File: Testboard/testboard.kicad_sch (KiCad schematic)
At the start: 0 parts

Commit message: :sparkles: Create the schematic for the testboard
Mostly copied from the original schematic.
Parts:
- added C1, C3, C5, C6, C7: 100n, Capacitor_THT:C_Disc_D4.3mm_W1.9mm_P5.00mm, symbol Device:C
- added C2, C4: 10n, Capacitor_THT:C_Disc_D4.3mm_W1.9mm_P5.00mm, symbol Device:C
- added D1: rt, LED_THT:LED_D3.0mm, symbol Device:LED
- added J1: upper, Connector_PinSocket_2.54mm:PinSocket_2x02_P2.54mm_Vertical, symbol Connector_Generic:Conn_02x02_Odd_Even
- added J2: lower, Connector_PinSocket_2.54mm:PinSocket_2x02_P2.54mm_Vertical, symbol Connector_Generic:Conn_02x02_Odd_Even
- added J3, J4: Out, Connector_PinHeader_2.54mm:PinHeader_1x02_P2.54mm_Vertical, symbol Connector_Generic:Conn_01x02
- added J5: V_{drive}, Connector_PinHeader_2.54mm:PinHeader_1x02_P2.54mm_Vertical, symbol Connector_Generic:Conn_01x02
- added Q1: BC547, Package_TO_SOT_THT:TO-92_Inline, symbol Transistor_BJT:BC547
- added R1: 100R, Resistor_THT:R_Axial_DIN0207_L6.3mm_D2.5mm_P7.62mm_Horizontal, symbol Device:R
- added R10, R9: 1k, Resistor_THT:R_Axial_DIN0207_L6.3mm_D2.5mm_P7.62mm_Horizontal, symbol Device:R
- added R2, R7: 2k2, Resistor_THT:R_Axial_DIN0207_L6.3mm_D2.5mm_P7.62mm_Horizontal, symbol Device:R
- added R3, R4, R8: 10k, Resistor_THT:R_Axial_DIN0207_L6.3mm_D2.5mm_P7.62mm_Horizontal, symbol Device:R
- added R5: 4k7, Resistor_THT:R_Axial_DIN0207_L6.3mm_D2.5mm_P7.62mm_Horizontal, symbol Device:R
- added R6: 470R, Resistor_THT:R_Axial_DIN0207_L6.3mm_D2.5mm_P7.62mm_Horizontal, symbol Device:R
- added RV1: 1M, Potentiometer_THT:Potentiometer_Piher_PT-10-V10_Vertical, symbol Device:R_Potentiometer
- added SW1: SW_Push, Button_Switch_Keyboard:SW_Cherry_MX_1.00u_PCB, symbol Switch:SW_Push
- added SW2: ON/ON, moPsy:PB_Hor_7x7_2pole_2.5mm, symbol Switch:SW_SPDT
- added TP1: IN, TestPoint:TestPoint_Loop_D1.80mm_Drill1.0mm_Beaded, symbol Connector:TestPoint
- added TP2: TRIGGER_IN, TestPoint:TestPoint_Loop_D1.80mm_Drill1.0mm_Beaded, symbol Connector:TestPoint
- added TP3: TR, TestPoint:TestPoint_Loop_D1.80mm_Drill1.0mm_Beaded, symbol Connector:TestPoint
- added TP4: TRIGGER_OUT, TestPoint:TestPoint_Loop_D1.80mm_Drill1.0mm_Beaded, symbol Connector:TestPoint
- added TP5: OUT, TestPoint:TestPoint_Loop_D1.80mm_Drill1.0mm_Beaded, symbol Connector:TestPoint
- added U1: LM555xN, Package_DIP:DIP-8_W7.62mm, symbol Timer:LM555xN
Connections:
- new net: Q1.2 (B), R7.2
- new net: C3.1, R4.1, U1.4 (R)
- new net: Q1.3 (E), R10.1, R8.2, R9.1
- new net: C5.1, C6.1, R5.1, U1.6 (THR), U1.7 (DIS)
- new net: D1.2 (A), R6.1
- new net: R5.2, RV1.2
- new net: J4.1 (Pin_1), R10.2
- new net: C2.2, R3.1, SW2.2 (B), TP3.1, U1.2 (TR)
- new net: R1.1, SW1.2, TP1.1
- new net: J3.1 (Pin_1), R9.2, TP5.1
- new net: C4.1, U1.5 (CV)
- new net: J5.2 (Pin_2), Q1.1 (C)
- new net +12V: C7.1, J1.3 (Pin_3), J1.4 (Pin_4), J5.1 (Pin_1), R2.2, R3.2, R4.2, RV1.1, U1.8 (VCC)
- new net GND: C1.1, C3.2, C4.2, C5.2, C6.2, C7.2, D1.1 (K), J2.1 (Pin_1), J2.2 (Pin_2), J3.2 (Pin_2), J4.2 (Pin_2), R8.1, SW1.1, U1.1 (GND)
- new net TRIGGER_IN: C1.2, C2.1, R1.2, R2.1, SW2.1 (A), TP2.1
- new net TRIGGER_OUT: R6.2, R7.1, TP4.1, U1.3 (Q)
- no-connect marks 0 -> 6
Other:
- note added: "1ms - 250ms"
- note added: "Close to disable HPF, enables Gate mode"
- note added: "Gate/Trigger Output"
- note added: "HPF"
- note added: "LPF"
- note added: "Manual Input"
- note added: "Min Gate / Trigger Length"
- note added: "Power Supply"
- note added: "Trigger Length Selector"
- note added: "pull-up at the gate generator"

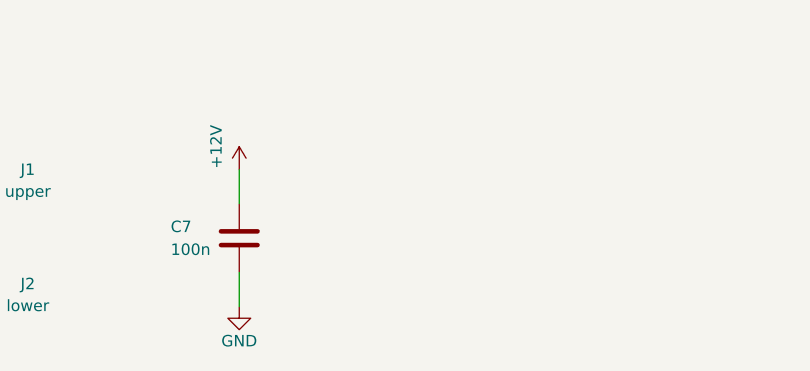
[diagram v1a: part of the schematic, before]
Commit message: :art: Add a GND testpoint for oscilloscope measurements
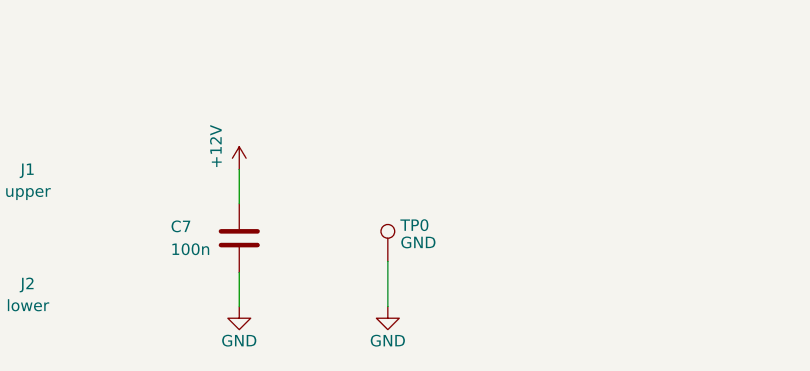
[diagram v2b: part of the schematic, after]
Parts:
- added TP0: GND, TestPoint:TestPoint_Loop_D1.80mm_Drill1.0mm_Beaded, symbol Connector:TestPoint
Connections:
- net GND: now also TP0.1
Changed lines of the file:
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@@
+    (stroke (width 0) (type default))
+  )
+  (wire (pts (xy 97.155 170.18) (xy 97.155 175.26))
     (stroke (width 0) (type default))
   )
@@
         (path "/64d6412c-bfad-42df-9ed7-bcc6cbff0470/a8014c65-0c58-4251-9031-5c5e91cdfe2c"
           (reference "RV7") (unit 1)
+        )
+      )
+    )
+  )
+  (symbol (lib_id "Connector:TestPoint") (at 97.155 170.18 0) (unit 1)
+    (in_bom yes) (on_board yes) (dnp no) (fields_autoplaced)
+    (property "Reference" "TP0" (at 98.552 166.2343 0)
+      (effects (font (size 1.27 1.27)) (justify left))
+    )
+    (property "Value" "GND" (at 98.552 168.1553 0)
+      (effects (font (size 1.27 1.27)) (justify left))
+    )
+    (property "Footprint" "TestPoint:TestPoint_Loop_D1.80mm_Drill1.0mm_Beaded" (at 102.235 170.18 0)
+      (effects (font (size 1.27 1.27)) hide)
+    )
+    (property "Datasheet" "~" (at 102.235 170.18 0)
+      (effects (font (size 1.27 1.27)) hide)
+    )
+    (pin "1")
+    (instances
+      (project "testboard"
+        (path "/1c5578e4-330a-41ae-a1d1-d71bb4a1a163"
+          (reference "TP0") (unit 1)
         )
       )
@@
         )
       )
+    )
+  )
+  (symbol (lib_id "power:GND") (at 97.155 175.26 0) (unit 1)
+    (in_bom yes) (on_board yes) (dnp no)
+    (property "Reference" "#PWR011" (at 97.155 181.61 0)
+      (effects (font (size 1.27 1.27)) hide)
+    )
+    (property "Value" "GND" (at 97.155 179.07 0)
+      (effects (font (size 1.27 1.27)))
+    )
+    (property "Footprint" "" (at 97.155 175.26 0)
+      (effects (font (size 1.27 1.27)) hide)
+    )
+    (property "Datasheet" "" (at 97.155 175.26 0)
+      (effects (font (size 1.27 1.27)) hide)
+    )
+    (pin "1")
+    (instances
+      (project "eurorack-power-breakout"
+        (path "/18b717ae-c948-4f75-a5e6-e6afbe279fcf"
+          (reference "#PWR011") (unit 1)
+        )
+      )
+      (project "testboard"
+        (path "/1c5578e4-330a-41ae-a1d1-d71bb4a1a163"
+          (reference "#PWR012") (unit 1)
+        )
+      )

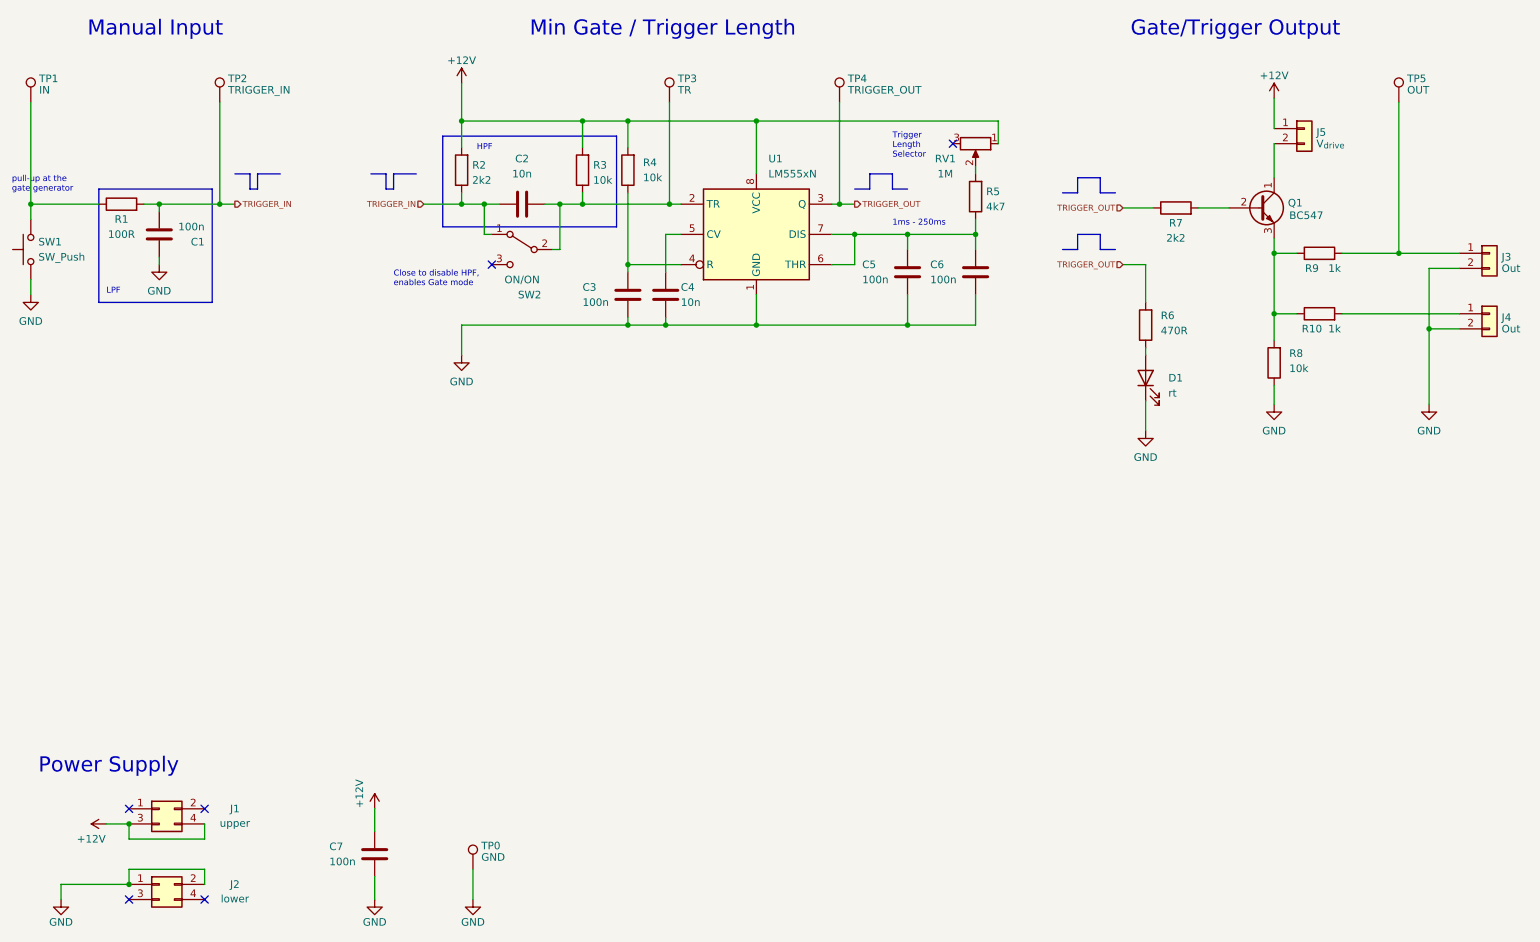
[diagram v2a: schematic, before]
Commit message: :art: Use +5V input as V_drive
If the pwr breakout is not set correctly, V_drive will be GND, but
not lead to any issues.
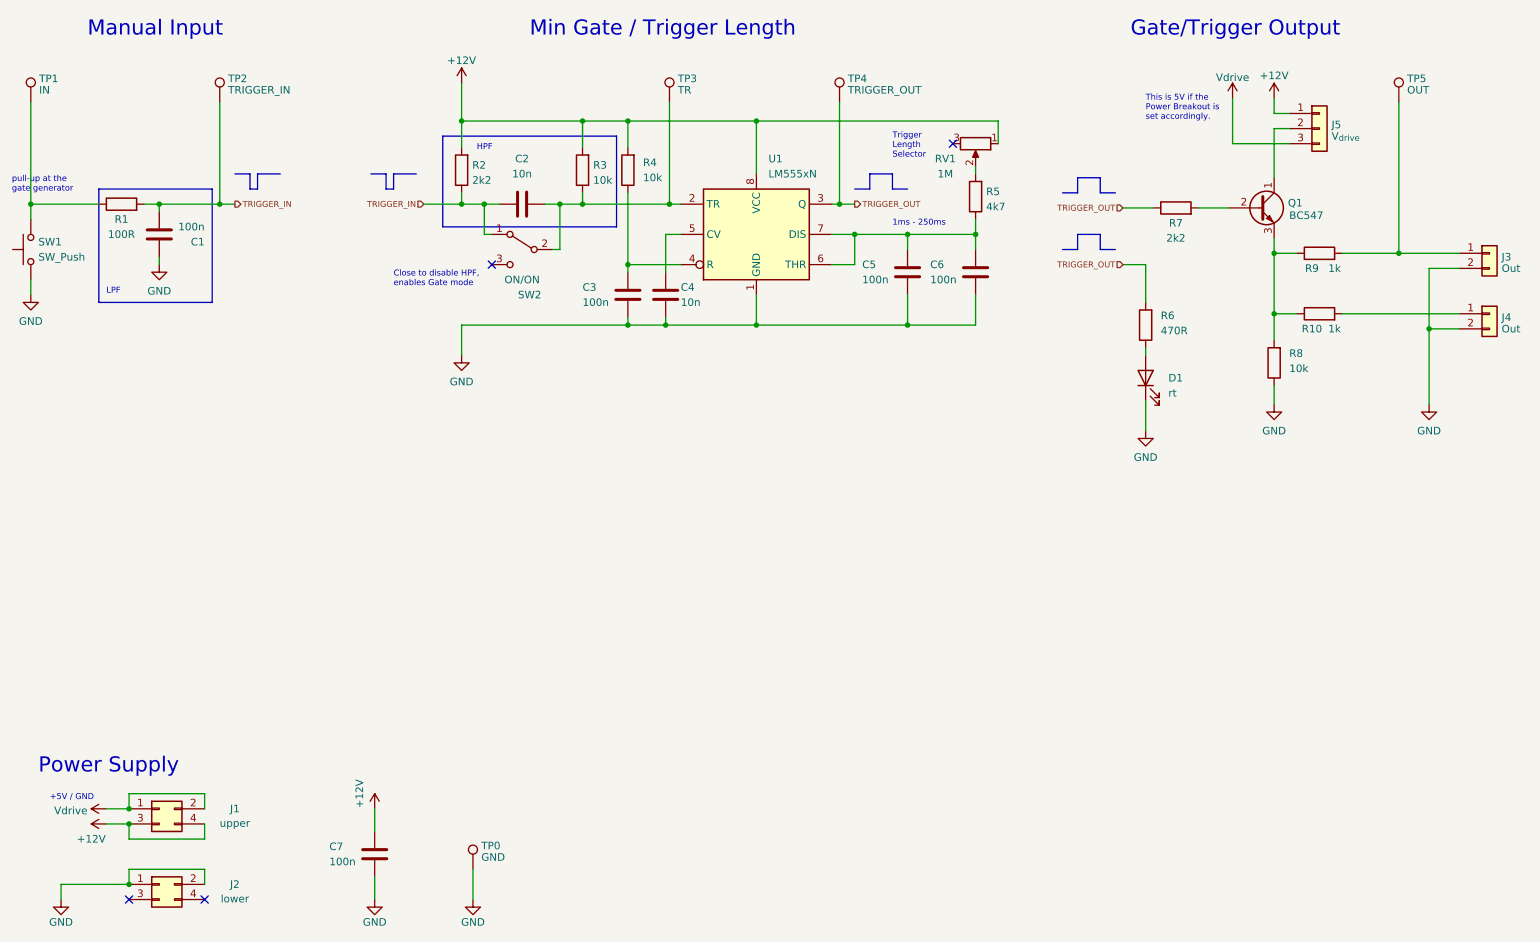
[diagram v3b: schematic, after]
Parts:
- J5: footprint Connector_PinHeader_2.54mm:PinHeader_1x02_P2.54mm_Vertical -> Connector_PinHeader_2.54mm:PinHeader_1x03_P2.54mm_Vertical; symbol Connector_Generic:Conn_01x02 -> Connector_Generic:Conn_01x03
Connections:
- net Vdrive: now reaches J1.1 (Pin_1)
- net Vdrive: now also J1.2 (Pin_2), J5.3 (Pin_3)
- no-connect marks 6 -> 4
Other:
- note added: "+5V / GND"
- note added: "This is 5V if the Power Breakout is set accordingly."
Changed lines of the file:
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@@
   (junction (at 95.25 44.45) (diameter 0) (color 0 0 0 0)
+  )
+  (junction (at 39.37 160.02) (diameter 0) (color 0 0 0 0)
   )
   (junction (at 181.61 63.5) (diameter 0) (color 0 0 0 0)
@@
   (no_connect (at 100.33 68.58))
   (no_connect (at 39.37 175.26))
-  (no_connect (at 52.07 160.02))
   (no_connect (at 52.07 175.26))
-  (no_connect (at 39.37 160.02))
   (no_connect (at 177.8 48.26))
   (polyline (pts (xy 202.565 66.04) (xy 202.565 63.5))
@@
     (stroke (width 0) (type default))
   )
+  (wire (pts (xy 234.315 48.26) (xy 224.79 48.26))
+    (stroke (width 0) (type default))
+  )
   (wire (pts (xy 52.07 162.56) (xy 52.07 165.1))
     (stroke (width 0) (type default))
@@
     (stroke (width 0) (type default))
   )
+  (wire (pts (xy 224.79 48.26) (xy 224.79 40.64))
+    (stroke (width 0) (type default))
+  )
   (polyline (pts (xy 83.82 53.34) (xy 87.63 53.34))
     (stroke (width 0) (type solid))
@@
     (stroke (width 0) (type solid))
   )
-  (wire (pts (xy 231.775 48.26) (xy 231.775 53.975))
-    (stroke (width 0) (type default))
-  )
   (wire (pts (xy 206.375 68.58) (xy 210.185 68.58))
     (stroke (width 0) (type default))
@@
     (stroke (width 0) (type default))
   )
-  (wire (pts (xy 231.775 40.64) (xy 231.775 45.72))
-    (stroke (width 0) (type default))
-  )
   (wire (pts (xy 181.61 60.96) (xy 181.61 63.5))
     (stroke (width 0) (type default))
@@
     (stroke (width 0) (type default))
   )
+  (wire (pts (xy 231.775 43.18) (xy 234.315 43.18))
+    (stroke (width 0) (type default))
+  )
   (wire (pts (xy 129.54 63.5) (xy 129.54 69.85))
     (stroke (width 0) (type default))
@@
     (stroke (width 0) (type default))
   )
+  (wire (pts (xy 35.56 160.02) (xy 39.37 160.02))
+    (stroke (width 0) (type default))
+  )
   (polyline (pts (xy 202.565 53.975) (xy 198.755 53.975))
     (stroke (width 0) (type solid))
@@
     (stroke (width 0) (type solid))
   )
+  (wire (pts (xy 231.775 45.72) (xy 234.315 45.72))
+    (stroke (width 0) (type default))
+  )
   (wire (pts (xy 115.57 56.515) (xy 115.57 58.42))
     (stroke (width 0) (type default))
@@
     (stroke (width 0) (type default))
   )
+  (wire (pts (xy 231.775 53.975) (xy 231.775 45.72))
+    (stroke (width 0) (type default))
+  )
+  (wire (pts (xy 231.775 40.64) (xy 231.775 43.18))
+    (stroke (width 0) (type default))
+  )
   (wire (pts (xy 115.57 44.45) (xy 123.19 44.45))
     (stroke (width 0) (type default))
@@
     (stroke (width 0) (type default))
   )
+  (wire (pts (xy 52.07 157.48) (xy 39.37 157.48))
+    (stroke (width 0) (type default))
+  )
   (wire (pts (xy 161.29 63.5) (xy 170.18 63.5))
     (stroke (width 0) (type default))
@@
   )
   (wire (pts (xy 95.25 58.42) (xy 99.06 58.42))
+    (stroke (width 0) (type default))
+  )
+  (wire (pts (xy 39.37 157.48) (xy 39.37 160.02))
+    (stroke (width 0) (type default))
+  )
+  (wire (pts (xy 52.07 160.02) (xy 52.07 157.48))
     (stroke (width 0) (type default))
   )
@@
   )
   (text "Trigger\nLength\nSelector" (at 167.64 50.8 0)
+    (effects (font (size 1 1)) (justify left bottom))
+  )
+  (text "This is 5V if the \nPower Breakout is\nset accordingly."
+    (at 210.185 44.45 0)
+    (effects (font (size 1 1)) (justify left bottom))
+  )
+  (text "+5V / GND" (at 26.035 158.75 0)
     (effects (font (size 1 1)) (justify left bottom))
   )
@@
         (path "/64d6412c-bfad-42df-9ed7-bcc6cbff0470/05164ba2-60fe-4a23-ac8d-eb46fec4725a"
           (reference "C34") (unit 1)
+        )
+      )
+    )
+  )
+  (symbol (lib_id "power:Vdrive") (at 224.79 40.64 0) (unit 1)
+    (in_bom yes) (on_board yes) (dnp no) (fields_autoplaced)
+    (property "Reference" "#PWR015" (at 219.71 44.45 0)
+      (effects (font (size 1.27 1.27)) hide)
+    )
+    (property "Value" "Vdrive" (at 224.79 37.1381 0)
+      (effects (font (size 1.27 1.27)))
+    )
+    (property "Footprint" "" (at 224.79 40.64 0)
+      (effects (font (size 1.27 1.27)) hide)
+    )
+    (property "Datasheet" "" (at 224.79 40.64 0)
+      (effects (font (size 1.27 1.27)) hide)
+    )
+    (pin "1")
+    (instances
+      (project "testboard"
+        (path "/1c5578e4-330a-41ae-a1d1-d71bb4a1a163"
+          (reference "#PWR015") (unit 1)
         )
       )
@@
     )
   )
+  (symbol (lib_id "power:Vdrive") (at 35.56 160.02 90) (unit 1)
+    (in_bom yes) (on_board yes) (dnp no) (fields_autoplaced)
+    (property "Reference" "#PWR014" (at 39.37 165.1 0)
+      (effects (font (size 1.27 1.27)) hide)
+    )
+    (property "Value" "Vdrive" (at 32.385 160.3368 90)
+      (effects (font (size 1.27 1.27)) (justify left))
+    )
+    (property "Footprint" "" (at 35.56 160.02 0)
+      (effects (font (size 1.27 1.27)) hide)
+    )
+    (property "Datasheet" "" (at 35.56 160.02 0)
+      (effects (font (size 1.27 1.27)) hide)
+    )
+    (pin "1")
+    (instances
+      (project "testboard"
+        (path "/1c5578e4-330a-41ae-a1d1-d71bb4a1a163"
+          (reference "#PWR014") (unit 1)
+        )
+      )
+    )
+  )
   (symbol (lib_id "power:+12V") (at 80.645 160.02 0) (unit 1)
     (in_bom yes) (on_board yes) (dnp no)
@@
     )
   )
-  (symbol (lib_id "Connector_Generic:Conn_01x02") (at 236.855 45.72 0) (unit 1)
+  (symbol (lib_id "Connector_Generic:Conn_01x03") (at 239.395 45.72 0) (unit 1)
     (in_bom yes) (on_board yes) (dnp no) (fields_autoplaced)
-    (property "Reference" "J5" (at 238.887 46.3463 0)
-      (effects (font (size 1.27 1.27)) (justify left))
-    )
-    (property "Value" "V_{drive}" (at 238.887 48.2673 0)
-      (effects (font (size 1.27 1.27)) (justify left))
-    )
-    (property "Footprint" "Connector_PinHeader_2.54mm:PinHeader_1x02_P2.54mm_Vertical" (at 236.855 45.72 0)
-      (effects (font (size 1.27 1.27)) hide)
-    )
-    (property "Datasheet" "~" (at 236.855 45.72 0)
-      (effects (font (size 1.27 1.27)) hide)
-    )
-    (pin "1")
-    (pin "2")
-    (instances
-      (project "testboard"
+    (property "Reference" "J5" (at 241.427 45.0763 0)
+      (effects (font (size 1.27 1.27)) (justify left))
+    )
+    (property "Value" "V_{drive}" (at 241.427 46.9973 0)
+      (effects (font (size 1.27 1.27)) (justify left))
+    )
+    (property "Footprint" "Connector_PinHeader_2.54mm:PinHeader_1x03_P2.54mm_Vertical" (at 239.395 45.72 0)
+      (effects (font (size 1.27 1.27)) hide)
+    )
+    (property "Datasheet" "~" (at 239.395 45.72 0)
+      (effects (font (size 1.27 1.27)) hide)
+    )
+    (pin "1")
+    (pin "2")
+    (pin "3")
+    (instances
+      (project "testboard"
